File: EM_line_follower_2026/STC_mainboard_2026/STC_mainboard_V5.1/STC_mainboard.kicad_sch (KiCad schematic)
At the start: 113 parts, among them J1 Conn_01x04, J10 Conn_01x04, J11 WirePad, J12 WirePad, J13 Conn_01x02, J14 WirePad, J15 WirePad, J16 WirePad, J2 WirePad, J20 WirePad, J21 WirePad, J23 WirePad, J24 WirePad, J3 WirePad, J4 Conn_01x04, J5 WirePad, J6 WirePad, J7 WirePad, J8 WirePad, J9 Conn_01x04, SW1 SW_Push, SW3 SW_Push, U1 STC16H40K128_CoreBoard, U10 TPS54360DDA, U3 LSM6DSRTR, U4 LM1117-3.3V, U5 OPA2197xD, U6 OPA2197xD, U7 OPA2197xD

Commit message: update V5.1
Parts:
- removed J1: Conn_01x04, Connector_JST:JST_XH_B4B-XH-A_1x04_P2.50mm_Vertical, symbol STC:Conn_01x04
- added J17: Conn_02x04_Odd_Even, Connector_PinSocket_2.54mm:PinSocket_2x04_P2.54mm_Vertical, symbol Connector_Generic:Conn_02x04_Odd_Even
- added SW2, SW4: SW_Push, em1:SW-TH_L21.0-W15.0-KCD1-103, symbol Switch:SW_Push
- renumbered RV3 to L1, RV2 to L2, RV4 to L3, RV1 to L4, RV5 to L5, L1 to L7
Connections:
- net +12V: now also SW4.2; no longer 111.2 (+), J13.2 (Pin_2)
- net +5V: now also J17.8 (Pin_8), SW2.1; no longer U1.2 (VCC)
- net GND: now also J17.6 (Pin_6)
- net P5.2: now also J17.4 (Pin_4)
- net P5.3: now also J17.2 (Pin_2)
- net P0.7: now reaches U1.62 (0.7)
- net P0.7: now also J17.3 (Pin_3)
- new net: SW2.2, U1.2 (VCC)
- new net Vin: 111.2 (+), J13.2 (Pin_2), SW4.1
- no-connect marks 52 -> 54

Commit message: update wire(hole) position and step file as well
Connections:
- net at U6.5 (+): no longer R38.2
- net at L5.1, R26.1: now also U6.1; no longer U6.7
- net at L5.2, L5.3, R37.2: now also U6.2 (-); no longer U6.6 (-)
- net at U6.3 (+): now also R38.2

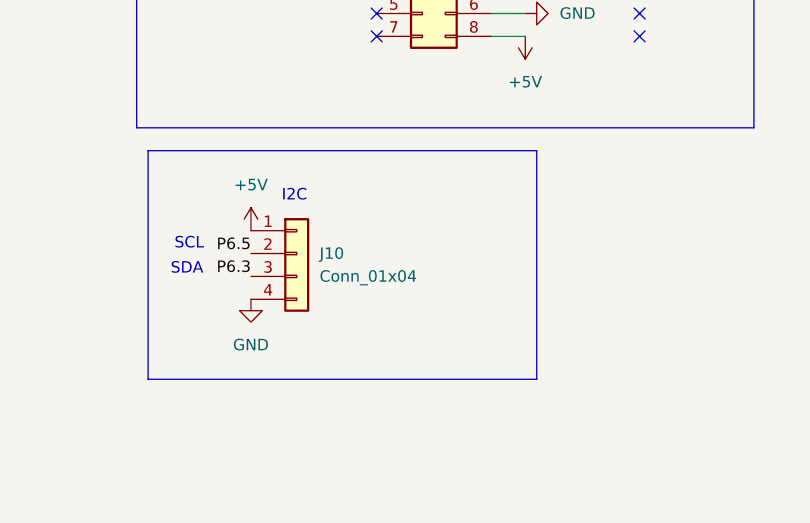
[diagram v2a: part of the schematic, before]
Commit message: update on board height
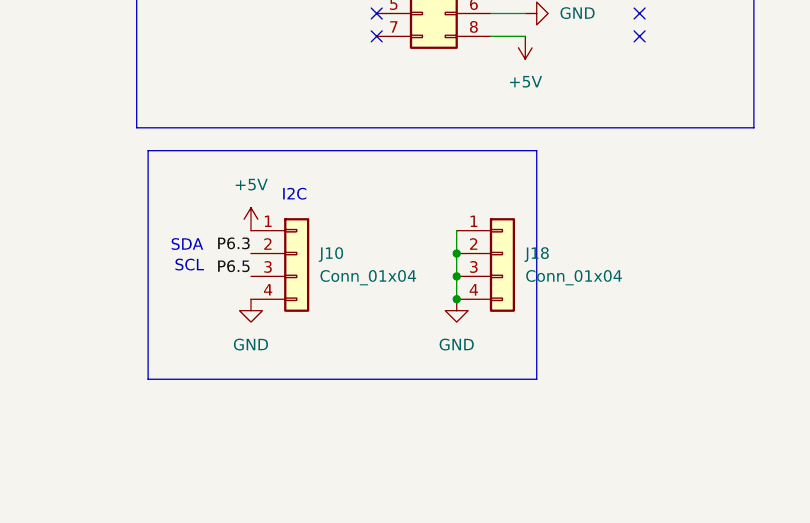
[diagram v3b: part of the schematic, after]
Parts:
- added J18: Conn_01x04, Connector_PinHeader_2.54mm:PinHeader_1x04_P2.54mm_Vertical, symbol STC:Conn_01x04
- J10: footprint Connector_JST:JST_XH_B4B-XH-A_1x04_P2.50mm_Vertical -> Connector_PinHeader_2.54mm:PinHeader_1x04_P2.54mm_Vertical
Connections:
- net GND: now also J18.1 (Pin_1), J18.2 (Pin_2), J18.3 (Pin_3), J18.4 (Pin_4)
- net P6.3: now also J10.2 (Pin_2); no longer J10.3 (Pin_3)
- net P6.5: now also J10.3 (Pin_3); no longer J10.2 (Pin_2)
